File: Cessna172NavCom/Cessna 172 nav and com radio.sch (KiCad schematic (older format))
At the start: 14 parts, among them J1 Conn_02x12_Odd_Even, SW1 COMM toggle, SW2 NAV toggle, SW5 Test switch, SW6 Ident switch

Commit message: Fix up paths
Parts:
- SW1, SW2, SW5, SW6: symbol Cessna~172~nav~and~com~radio:B3W-9000-xxx -> Cessna_172_nav_and_com_radio:B3W-9000-xxx
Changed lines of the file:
@@
 	5550 5900 5550 4700
 $Comp
-L Cessna~172~nav~and~com~radio:B3W-9000-xxx SW1
+L Cessna_172_nav_and_com_radio:B3W-9000-xxx SW1
 U 1 1 5F605163
 P 1100 5300
@@
 $EndComp
 $Comp
-L Cessna~172~nav~and~com~radio:B3W-9000-xxx SW2
+L Cessna_172_nav_and_com_radio:B3W-9000-xxx SW2
 U 1 1 5F6062D0
 P 2450 5300
@@
 $EndComp
 $Comp
-L Cessna~172~nav~and~com~radio:B3W-9000-xxx SW5
+L Cessna_172_nav_and_com_radio:B3W-9000-xxx SW5
 U 1 1 5F607045
 P 3700 5300
@@
 $EndComp
 $Comp
-L Cessna~172~nav~and~com~radio:B3W-9000-xxx SW6
+L Cessna_172_nav_and_com_radio:B3W-9000-xxx SW6
 U 1 1 5F6074D3
 P 4850 5300

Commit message: Traces for one LCD bank complete
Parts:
- removed SW5: Test switch, Cessna 172 nav and com radio:B3W-9000-xxx, symbol Cessna_172_nav_and_com_radio:B3W-9000-xxx
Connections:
- net labels removed: COMM_VOL_SW
- wire segments 56 -> 53
- no-connect marks 12 -> 11
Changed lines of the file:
@@
 COMM_VOL_RIGHT
 Text GLabel 8950 1450 2    50   Output ~ 0
-COMM_VOL_SW
+TEST_SW
 Wire Wire Line
 	8850 1150 8950 1150
@@
 Wire Notes Line
 	4400 650  9700 650
-Text GLabel 3900 5550 2    50   Input ~ 0
-TEST_LED
-Text GLabel 3900 5350 2    50   Output ~ 0
-TEST_SW
 Wire Notes Line
 	600  4700 5550 4700
@@
 COMM_VOL_RIGHT
 Text GLabel 1900 2550 0    50   Input ~ 0
-COMM_VOL_SW
-Text GLabel 1900 2650 0    50   Input ~ 0
 IDENT_SW
-Text GLabel 1900 2750 0    50   Output ~ 0
+Text GLabel 1900 2650 0    50   Output ~ 0
 IDENT_LED
 NoConn ~ 2400 2650
@@
 NoConn ~ 2650 5150
 NoConn ~ 2250 5150
-Text GLabel 3450 5450 0    50   Input ~ 0
-GND
-Wire Wire Line
-	3500 5350 3500 5450
-Wire Wire Line
-	3500 5450 3450 5450
-Connection ~ 3500 5450
-Wire Wire Line
-	3500 5450 3500 5550
-NoConn ~ 3900 5150
-NoConn ~ 3500 5150
 NoConn ~ 4650 5150
 NoConn ~ 5050 5150
@@
 $EndComp
 $Comp
-L Cessna_172_nav_and_com_radio:B3W-9000-xxx SW5
-U 1 1 5F607045
-P 3700 5300
-F 0 "SW5" H 3700 5735 50  0000 C CNN
-F 1 "Test switch" H 3700 5644 50  0000 C CNN
-F 2 "Cessna 172 nav and com radio:B3W-9000-xxx" H 3700 5300 50  0001 C CNN
-F 3 "" H 3700 5300 50  0001 C CNN
-	1    3700 5300
-	1    0    0    -1
-$EndComp
-$Comp
 L Cessna_172_nav_and_com_radio:B3W-9000-xxx SW6
 U 1 1 5F6074D3
@@
 $EndComp
 NoConn ~ 1400 3950
+NoConn ~ 1900 2750
 $EndSCHEMATC

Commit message: LEDs and power jack
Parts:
- removed R13: 220, Resistor_SMD:R_0805_2012Metric_Pad1.15x1.40mm_HandSolder, symbol Device:R
- added D2: LED, LED_SMD:LED_0805_2012Metric_Pad1.15x1.40mm_HandSolder, symbol Device:LED
- added J2: Conn_01x05, Connector_PinHeader_2.54mm:PinHeader_1x05_P2.54mm_Vertical, symbol Connector_Generic:Conn_01x05
- added J3: Barrel_Jack_MountingPin, Cessna 172 nav and com radio:BarrelJack_Horizontal, symbol Connector:Barrel_Jack_MountingPin
- added R2, R3: 220k, Resistor_SMD:R_0805_2012Metric_Pad1.15x1.40mm_HandSolder, symbol Device:R
- D1: footprint LED_SMD:LED_0805_2012Metric_Pad1.15x1.40mm_HandSolder -> LED_THT:LED_D5.0mm
- R1: value 220 -> 220k
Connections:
- net labels added: DOUT
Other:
- note added: "Status LEDs"
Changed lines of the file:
@@
 Text Notes 7450 3400 0    50   ~ 0
 NAV standby
-NoConn ~ 8900 3800
 Wire Wire Line
 	8750 3800 8900 3800
@@
 Wire Notes Line
 	4400 650  9700 650
-Wire Notes Line
-	600  4700 5550 4700
-$Comp
-L Device:LED D1
-U 1 1 5F5F30E5
-P 3650 900
-F 0 "D1" H 3750 1000 50  0000 C CNN
-F 1 "LED" H 3750 1100 50  0000 C CNN
-F 2 "LED_SMD:LED_0805_2012Metric_Pad1.15x1.40mm_HandSolder" H 3650 900 50  0001 C CNN
-F 3 "~" H 3650 900 50  0001 C CNN
-	1    3650 900
-	-1   0    0    1
-$EndComp
-$Comp
-L Device:R R13
-U 1 1 5F5F4214
-P 3800 1050
-F 0 "R13" H 3870 1096 50  0000 L CNN
-F 1 "220" H 3870 1005 50  0000 L CNN
-F 2 "Resistor_SMD:R_0805_2012Metric_Pad1.15x1.40mm_HandSolder" V 3730 1050 50  0001 C CNN
-F 3 "~" H 3800 1050 50  0001 C CNN
-	1    3800 1050
-	1    0    0    -1
-$EndComp
 Connection ~ 3200 1200
-Connection ~ 3800 1200
-Wire Wire Line
-	3800 1200 4100 1200
 Connection ~ 3200 900
-Wire Wire Line
-	3800 900  4100 900
-Connection ~ 3800 900
-Wire Wire Line
-	3200 1200 3800 1200
-Wire Wire Line
-	3200 900  3500 900
 Wire Wire Line
 	3150 900  3200 900
@@
 Wire Wire Line
 	2000 3900 2100 3900
-Wire Notes Line
-	9000 3050 9000 4450
-Wire Notes Line
-	600  4450 9000 4450
-Wire Notes Line
-	600  3050 9000 3050
 $Comp
 L Device:R R1
@@
 P 1250 3650
 F 0 "R1" H 1320 3696 50  0000 L CNN
-F 1 "220" H 1320 3605 50  0000 L CNN
+F 1 "220k" H 1320 3605 50  0000 L CNN
 F 2 "Resistor_SMD:R_0805_2012Metric_Pad1.15x1.40mm_HandSolder" V 1180 3650 50  0001 C CNN
 F 3 "~" H 1250 3650 50  0001 C CNN
@@
 NoConn ~ 2650 5150
 NoConn ~ 2250 5150
-NoConn ~ 4650 5150
-NoConn ~ 5050 5150
-Wire Wire Line
-	4650 5450 4650 5550
-Connection ~ 4650 5450
-Wire Wire Line
-	4650 5450 4600 5450
-Wire Wire Line
-	4650 5350 4650 5450
-Text GLabel 4600 5450 0    50   Input ~ 0
-GND
-Wire Notes Line
-	600  5900 5550 5900
-Text GLabel 5050 5350 2    50   Output ~ 0
+NoConn ~ 3500 5150
+NoConn ~ 3900 5150
+Wire Wire Line
+	3500 5450 3500 5550
+Connection ~ 3500 5450
+Wire Wire Line
+	3500 5450 3450 5450
+Wire Wire Line
+	3500 5350 3500 5450
+Text GLabel 3450 5450 0    50   Input ~ 0
+GND
+Text GLabel 3900 5350 2    50   Output ~ 0
 IDENT_SW
-Text GLabel 5050 5550 2    50   Input ~ 0
+Text GLabel 3900 5550 2    50   Input ~ 0
 IDENT_LED
-Wire Notes Line
-	5550 5900 5550 4700
 $Comp
 L Cessna_172_nav_and_com_radio:B3W-9000-xxx SW1
@@
 L Cessna_172_nav_and_com_radio:B3W-9000-xxx SW6
 U 1 1 5F6074D3
-P 4850 5300
-F 0 "SW6" H 4850 5735 50  0000 C CNN
-F 1 "Ident switch" H 4850 5644 50  0000 C CNN
-F 2 "Cessna 172 nav and com radio:B3W-9000-xxx" H 4850 5300 50  0001 C CNN
-F 3 "" H 4850 5300 50  0001 C CNN
-	1    4850 5300
+P 3700 5300
+F 0 "SW6" H 3700 5735 50  0000 C CNN
+F 1 "Ident switch" H 3700 5644 50  0000 C CNN
+F 2 "Cessna 172 nav and com radio:B3W-9000-xxx" H 3700 5300 50  0001 C CNN
+F 3 "" H 3700 5300 50  0001 C CNN
+	1    3700 5300
 	1    0    0    -1
 $EndComp
 NoConn ~ 1400 3950
 NoConn ~ 1900 2750
+$Comp
+L Connector_Generic:Conn_01x05 J2
+U 1 1 5F5E75F2
+P 3750 1850
+F 0 "J2" H 3700 2250 50  0000 L CNN
+F 1 "Conn_01x05" H 3500 2150 50  0000 L CNN
+F 2 "Connector_PinHeader_2.54mm:PinHeader_1x05_P2.54mm_Vertical" H 3750 1850 50  0001 C CNN
+F 3 "~" H 3750 1850 50  0001 C CNN
+	1    3750 1850
+	1    0    0    -1
+$EndComp
+Text GLabel 3550 1650 0    50   Output ~ 0
++5V
+Text GLabel 3550 1750 0    50   Output ~ 0
+GND
+Text GLabel 3550 1850 0    50   Output ~ 0
+LOAD
+Text GLabel 3550 1950 0    50   Output ~ 0
+CLK
+Text GLabel 3550 2050 0    50   Output ~ 0
+DOUT
+Text GLabel 8900 3800 2    50   Output ~ 0
+DOUT
+Wire Notes Line
+	9200 4450 9200 3050
+Wire Notes Line
+	600  4450 9200 4450
+Wire Notes Line
+	600  3050 9200 3050
+Wire Notes Line
+	600  4700 4400 4700
+Wire Notes Line
+	600  5900 4400 5900
+Wire Notes Line
+	4400 4700 4400 5900
+$Comp
+L Connector:Barrel_Jack_MountingPin J3
+U 1 1 5F5F8100
+P 3600 2500
+F 0 "J3" H 3657 2817 50  0000 C CNN
+F 1 "Barrel_Jack_MountingPin" H 3657 2726 50  0000 C CNN
+F 2 "Cessna 172 nav and com radio:BarrelJack_Horizontal" H 3650 2460 50  0001 C CNN
+F 3 "~" H 3650 2460 50  0001 C CNN
+	1    3600 2500
+	1    0    0    -1
+$EndComp
+NoConn ~ 3600 2800
+Text GLabel 3900 2400 2    50   Input ~ 0
++5V
+Text GLabel 3900 2600 2    50   Input ~ 0
+GND
+$Comp
+L Device:LED D1
+U 1 1 5F5FCD17
+P 4950 5400
+F 0 "D1" H 4943 5616 50  0000 C CNN
+F 1 "LED" H 4943 5525 50  0000 C CNN
+F 2 "LED_THT:LED_D5.0mm" H 4950 5400 50  0001 C CNN
+F 3 "~" H 4950 5400 50  0001 C CNN
+	1    4950 5400
+	0    -1   -1   0
+$EndComp
+Text GLabel 4950 5550 3    50   Input ~ 0
+GND
+Text GLabel 4600 5250 1    50   Input ~ 0
+TEST_LED
+Wire Notes Line
+	4450 4700 4450 5900
+Wire Notes Line
+	4450 5900 8150 5900
+Wire Notes Line
+	8150 5900 8150 4700
+Wire Notes Line
+	8150 4700 4450 4700
+Text Notes 4450 4650 0    50   ~ 0
+Status LEDs
+$Comp
+L Device:R R2
+U 1 1 5F608695
+P 4800 5250
+F 0 "R2" V 4593 5250 50  0000 C CNN
+F 1 "220k" V 4684 5250 50  0000 C CNN
+F 2 "Resistor_SMD:R_0805_2012Metric_Pad1.15x1.40mm_HandSolder" V 4730 5250 50  0001 C CNN
+F 3 "~" H 4800 5250 50  0001 C CNN
+	1    4800 5250
+	0    1    1    0
+$EndComp
+Wire Wire Line
+	4600 5250 4650 5250
+$Comp
+L Device:LED D2
+U 1 1 5F60E071
+P 5550 5400
+F 0 "D2" H 5543 5616 50  0000 C CNN
+F 1 "LED" H 5543 5525 50  0000 C CNN
+F 2 "LED_SMD:LED_0805_2012Metric_Pad1.15x1.40mm_HandSolder" H 5550 5400 50  0001 C CNN
+F 3 "~" H 5550 5400 50  0001 C CNN
+	1    5550 5400
+	0    -1   -1   0
+$EndComp
+Text GLabel 5550 5550 3    50   Input ~ 0
+GND
+Text GLabel 5200 5250 1    50   Input ~ 0
++5V
+$Comp
+L Device:R R3
+U 1 1 5F60E079
+P 5400 5250
+F 0 "R3" V 5193 5250 50  0000 C CNN
+F 1 "220k" V 5284 5250 50  0000 C CNN
+F 2 "Resistor_SMD:R_0805_2012Metric_Pad1.15x1.40mm_HandSolder" V 5330 5250 50  0001 C CNN
+F 3 "~" H 5400 5250 50  0001 C CNN
+	1    5400 5250
+	0    1    1    0
+$EndComp
+Wire Wire Line
+	5200 5250 5250 5250
+Wire Wire Line
+	3200 1200 4100 1200
+Wire Wire Line
+	3200 900  4100 900
 $EndSCHEMATC

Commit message: Re-work to use 5 digit LEDs
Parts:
- removed SW1: COMM toggle, Cessna 172 nav and com radio:B3W-9000-xxx, symbol Cessna_172_nav_and_com_radio:B3W-9000-xxx
- removed SW2: NAV toggle, Cessna 172 nav and com radio:B3W-9000-xxx, symbol Cessna_172_nav_and_com_radio:B3W-9000-xxx
- removed SW6: Ident switch, Cessna 172 nav and com radio:B3W-9000-xxx, symbol Cessna_172_nav_and_com_radio:B3W-9000-xxx
- added D3: LED, LED_THT:LED_D5.0mm, symbol Device:LED
- added R4: 220k, Resistor_SMD:R_0805_2012Metric_Pad1.15x1.40mm_HandSolder, symbol Device:R
- added SW1, SW2, SW3: SW_Push, Button_Switch_THT:SW_PUSH-12mm, symbol Switch:SW_Push
- renumbered D2 to D1, D1 to D2, J3 to J2, J2 to J3, R3 to R2, R2 to R3
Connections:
- net labels removed: COMM_TX_LED, NAV_TX_LED
- wire segments 53 -> 45
- no-connect marks 11 -> 7
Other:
- note added: "Test switch is on\nCOMM volume\nrotary encoder"
- moved on the sheet: D1, D2, R2, R3

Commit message: New board size!
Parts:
- SW1, SW2, SW3: footprint Button_Switch_THT:SW_PUSH-12mm -> Button_Switch_THT:SW_PUSH_6mm_H8mm
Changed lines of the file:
@@
 F 0 "SW1" H 1100 5385 50  0000 C CNN
 F 1 "SW_Push" H 1100 5294 50  0000 C CNN
-F 2 "Button_Switch_THT:SW_PUSH-12mm" H 1100 5300 50  0001 C CNN
+F 2 "Button_Switch_THT:SW_PUSH_6mm_H8mm" H 1100 5300 50  0001 C CNN
 F 3 "~" H 1100 5300 50  0001 C CNN
 	1    1100 5100
@@
 F 0 "SW2" H 1100 5835 50  0000 C CNN
 F 1 "SW_Push" H 1100 5744 50  0000 C CNN
-F 2 "Button_Switch_THT:SW_PUSH-12mm" H 1100 5750 50  0001 C CNN
+F 2 "Button_Switch_THT:SW_PUSH_6mm_H8mm" H 1100 5750 50  0001 C CNN
 F 3 "~" H 1100 5750 50  0001 C CNN
 	1    1100 5550
@@
 F 0 "SW3" H 2400 5385 50  0000 C CNN
 F 1 "SW_Push" H 2400 5294 50  0000 C CNN
-F 2 "Button_Switch_THT:SW_PUSH-12mm" H 2400 5300 50  0001 C CNN
+F 2 "Button_Switch_THT:SW_PUSH_6mm_H8mm" H 2400 5300 50  0001 C CNN
 F 3 "~" H 2400 5300 50  0001 C CNN
 	1    2400 5100

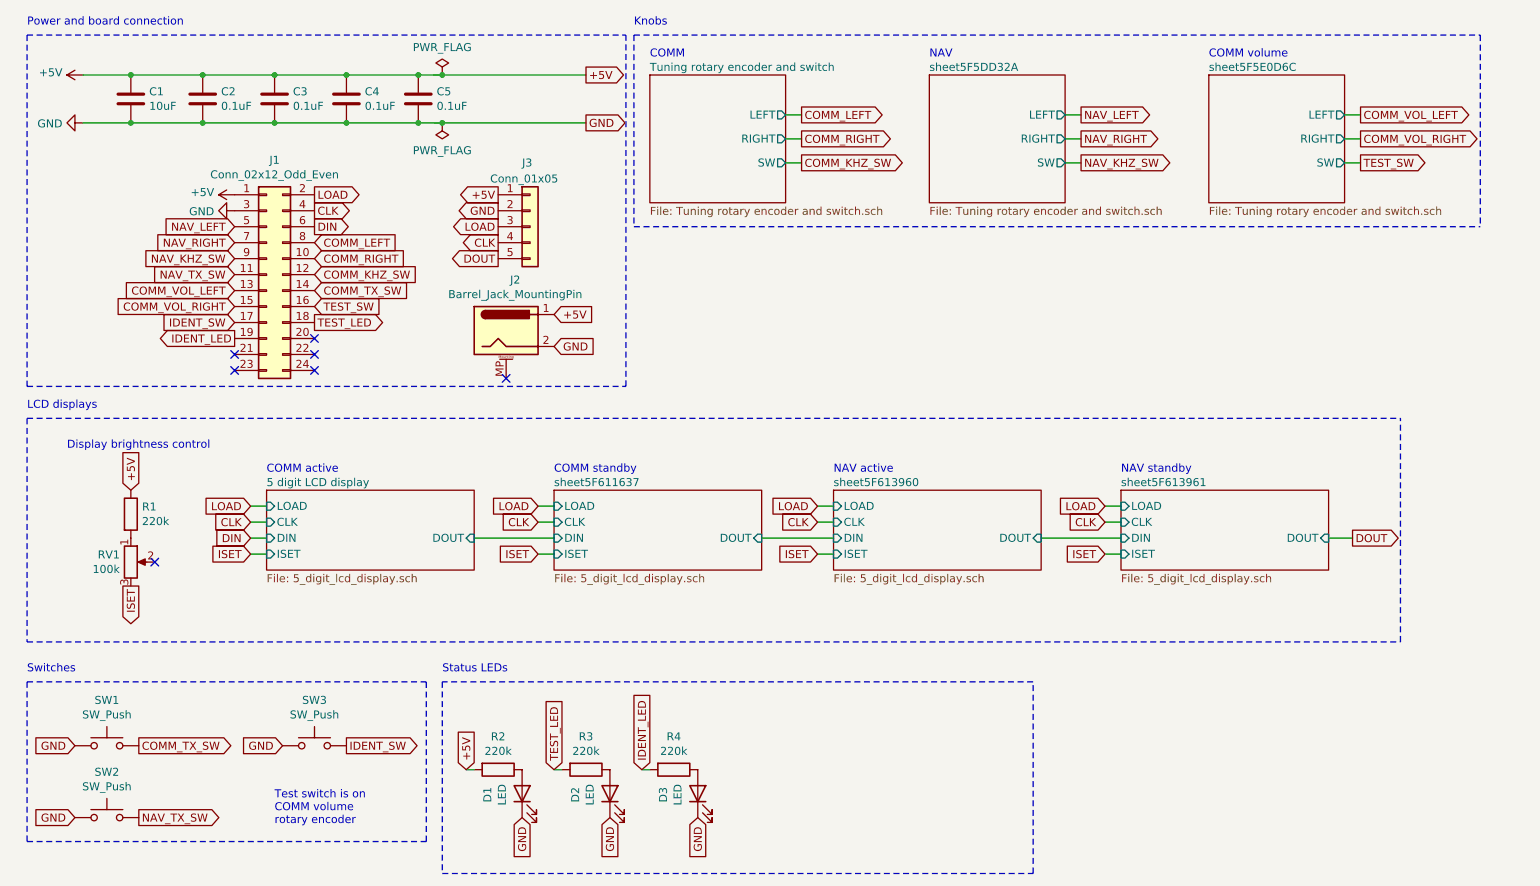
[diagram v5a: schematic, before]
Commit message: Switch to USB for power, all parts on board
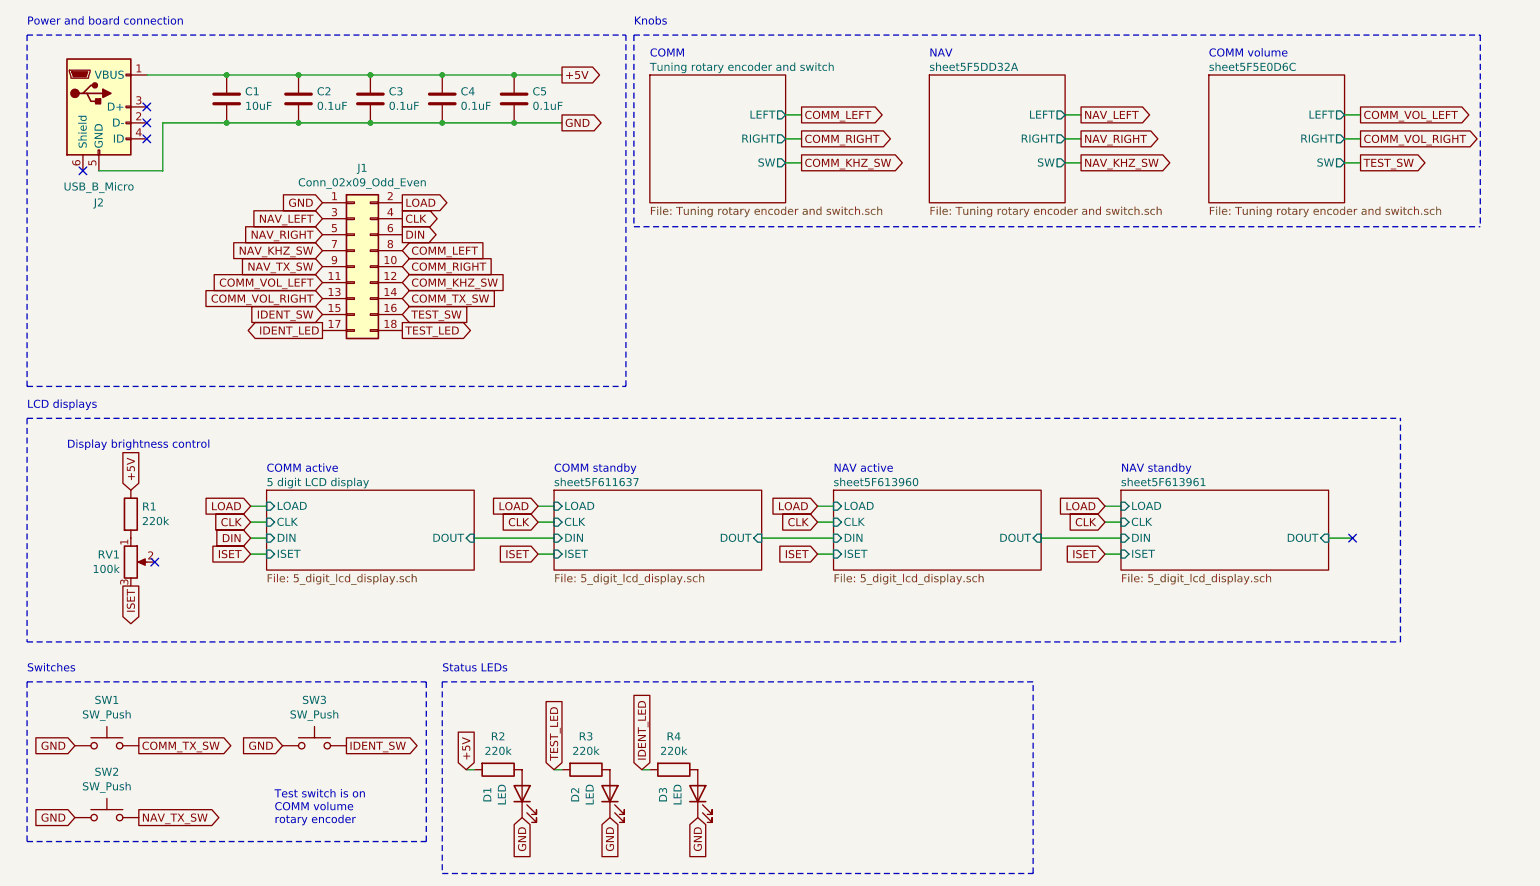
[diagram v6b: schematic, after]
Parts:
- removed J1: Conn_02x12_Odd_Even, Connector_PinHeader_2.54mm:PinHeader_2x12_P2.54mm_Vertical, symbol Connector_Generic:Conn_02x12_Odd_Even
- removed J2: Barrel_Jack_MountingPin, Cessna 172 nav and com radio:BarrelJack_Horizontal, symbol Connector:Barrel_Jack_MountingPin
- removed J3: Conn_01x05, Connector_PinHeader_2.54mm:PinHeader_1x05_P2.54mm_Vertical, symbol Connector_Generic:Conn_01x05
- added J1: Conn_02x09_Odd_Even, symbol Connector_Generic:Conn_02x09_Odd_Even
- added J2: USB_B_Micro, symbol Connector:USB_B_Micro
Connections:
- net labels removed: DOUT
- wire segments 45 -> 43
- no-connect marks 7 -> 6
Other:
- moved on the sheet: C1, C2, C3, C4, C5
